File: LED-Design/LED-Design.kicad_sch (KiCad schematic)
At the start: 160 parts, among them Q1 NMOS, Q2 NMOS, Q3 NMOS, Q4 NMOS, Q5 NMOS, Q6 NMOS, Q7 NMOS, U1 74HC574, U2 74HC574, U3 74HC574, U4 74HC574, U5 74HC164

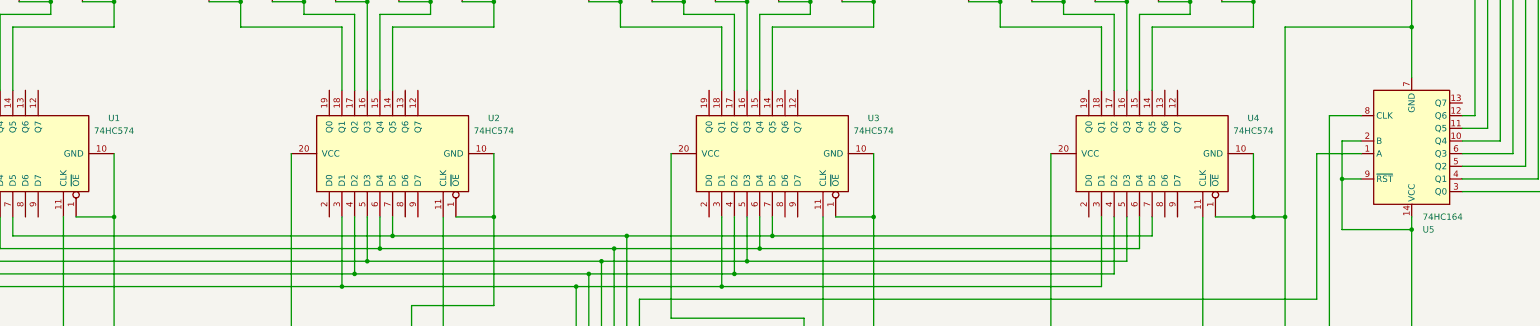
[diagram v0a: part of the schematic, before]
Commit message: Updated the schematics of Resistors and ICs to be linked to their footprints. Need to create a footprint for the MOSFETs
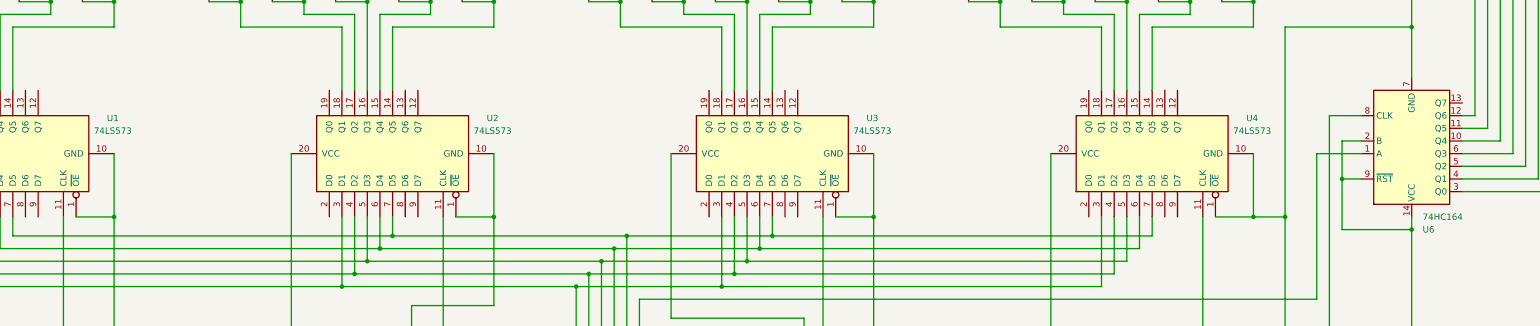
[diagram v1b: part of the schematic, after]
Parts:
- removed U5: 74HC164, symbol 74xx:74HC164
- added U6: 74HC164, Package_DIP:DIP-14_W7.62mm, symbol 74xx:74HC164
- R1, R2, R3, R4, R5, R6, R7: footprint (none) -> OptoDevice:R_LDR_5.2x5.2mm_P3.5mm_Horizontal
- U1, U2, U3, U4: value 74HC574 -> 74LS573; footprint (none) -> Package_DIP:DIP-20_W7.62mm
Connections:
- net +24V: now also U6.7 (GND)
- net at Q3.2 (G): now also U6.5 (Q2)
- net at A1.5 (D2): now also U6.1 (A)
- net at Q5.2 (G): now also U6.10 (Q4)
- net at Q6.2 (G): now also U6.11 (Q5)
- net at Q7.2 (G): now also U6.12 (Q6)
- net at A1.27 (+5V), U1.20 (VCC), U2.20 (VCC)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: now also U6.14 (VCC), U6.2 (B), U6.9 (~{RST})
- net at Q1.2 (G): now also U6.3 (Q0)
- net at Q2.2 (G): now also U6.4 (Q1)
- net at Q4.2 (G): now also U6.6 (Q3)
- net at A1.22 (A3): now also U6.8 (CLK)

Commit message: Added footprint for NMOS
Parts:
- Q1, Q2, Q3, Q4, Q5, Q6, Q7: footprint (none) -> Package_TO_SOT_THT:TO-220-3_Vertical
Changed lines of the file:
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@@
 			)
 		)
-		(property "Footprint" ""
+		(property "Footprint" "Package_TO_SOT_THT:TO-220-3_Vertical"
 			(at 353.06 78.74 0)
 			(effects
@@
 			)
 		)
-		(property "Footprint" ""
+		(property "Footprint" "Package_TO_SOT_THT:TO-220-3_Vertical"
 			(at 353.06 91.44 0)
 			(effects
@@
 			)
 		)
-		(property "Footprint" ""
+		(property "Footprint" "Package_TO_SOT_THT:TO-220-3_Vertical"
 			(at 353.06 116.84 0)
 			(effects
@@
 			)
 		)
-		(property "Footprint" ""
+		(property "Footprint" "Package_TO_SOT_THT:TO-220-3_Vertical"
 			(at 353.06 129.54 0)
 			(effects
@@
 			)
 		)
-		(property "Footprint" ""
+		(property "Footprint" "Package_TO_SOT_THT:TO-220-3_Vertical"
 			(at 353.06 66.04 0)
 			(effects
@@
 			)
 		)
-		(property "Footprint" ""
+		(property "Footprint" "Package_TO_SOT_THT:TO-220-3_Vertical"
 			(at 353.06 53.34 0)
 			(effects
@@
 			)
 		)
-		(property "Footprint" ""
+		(property "Footprint" "Package_TO_SOT_THT:TO-220-3_Vertical"
 			(at 353.06 104.14 0)
 			(effects

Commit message: Pulled from Shadab
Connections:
- net +24V: no longer Q1.3 (S), Q2.3 (S), Q3.3 (S), Q4.3 (S), Q5.3 (S), Q6.3 (S), Q7.3 (S), U1.1 (~{OE}), U1.10 (GND), U2.1 (~{OE}), U2.10 (GND), U3.1 (~{OE}), U3.10 (GND), U4.1 (~{OE}), U4.10 (GND), U6.7 (GND)
- new net GND: Q1.3 (S), Q2.3 (S), Q3.3 (S), Q4.3 (S), Q5.3 (S), Q6.3 (S), Q7.3 (S), U1.1 (~{OE}), U1.10 (GND), U2.1 (~{OE}), U2.10 (GND), U3.1 (~{OE}), U3.10 (GND), U4.1 (~{OE}), U4.10 (GND), U6.7 (GND)
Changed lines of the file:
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@@
 	)
 	(junction
-		(at 200.66 38.1)
-		(diameter 0)
-		(color 0 0 0 0)
-	)
-	(junction
 		(at 127 88.9)
 		(diameter 0)
@@
 	)
 	(junction
-		(at 368.3 38.1)
-		(diameter 0)
-		(color 0 0 0 0)
-	)
-	(junction
 		(at 285.75 134.62)
 		(diameter 0)
@@
 	(wire
 		(pts
-			(xy 368.3 31.75) (xy 368.3 38.1)
+			(xy 368.3 31.75) (xy 368.3 50.8)
 		)
 		(stroke
@@
 	(wire
 		(pts
-			(xy 200.66 38.1) (xy 368.3 38.1)
-		)
-		(stroke
-			(width 0)
-			(type default)
-		)
-	)
-	(wire
-		(pts
 			(xy 240.03 152.4) (xy 240.03 139.7)
 		)
@@
 		)
 		(stroke
-			(width 0)
-			(type default)
-		)
-	)
-	(wire
-		(pts
-			(xy 368.3 50.8) (xy 368.3 38.1)
-		)
-		(stroke
